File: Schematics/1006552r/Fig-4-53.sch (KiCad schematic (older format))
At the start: 46 parts, among them J1 ConnectorGeneric, U601 D3NOR-+3VDC-0VDC-nd1021041-_B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, U602 D3NOR-+3VDC-0VDC-nd1021041-_B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, U603 D3NOR-+3VDC-0VDC-nd1021041-_B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, U604 D3NOR-+3VDC-0VDC-nd1021041-AB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, U605 D3NOR-+3VDC-0VDC-nd1021041-AB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, U606 D3NOR-+3VDC-0VDC-nd1021041-AB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, U607 D3NOR-+3VDC-0VDC-nd1021041-CB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, U608 D3NOR-+3VDC-0VDC-nd1021041-_B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, U609 D3NOR-+3VDC-0VDC-nd1021041-AB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, U610 D3NOR-+3VDC-0VDC-nd1021041-AB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, U611 D3NOR-+3VDC-0VDC-nd1021041-_B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, U612 D3NOR-+3VDC-0VDC-nd1021041-_B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, U613 D3NOR-+3VDC-0VDC-nd1021041-CB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, U614 D3NOR-+3VDC-0VDC-nd1021041-_B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, U615 D3NOR-+3VDC-0VDC-nd1021041-AB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, U616 D3NOR-+3VDC-0VDC-nd1021041-_B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, U617 D3NOR-+3VDC-0VDC-nd1021041-_B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, U618 D3NOR-+3VDC-0VDC-nd1021041-_B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, U619 D3NOR-NC-0VDC-expander-nd1021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, U620 D3NOR-+3VDC-0VDC-nd1021041-_B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, U621 D3NOR-+3VDC-0VDC-nd1021041-AB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, U622 D3NOR-+3VDC-0VDC-nd1021041-_B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, U623 D3NOR-+3VDC-0VDC-nd1021041-_B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, U624 D3NOR-+3VDC-0VDC-nd1021041-_B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, U625 D3NOR-+3VDC-0VDC-nd1021041-_B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, U626 D3NOR-+3VDC-0VDC-nd1021041-_B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, U627 D3NOR-+3VDC-0VDC-nd1021041-_B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, U628 D3NOR-NC-0VDC-expander-nd1021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, U629 D3NOR-+3VDC-0VDC-nd1021041-_B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, U630 D3NOR-+3VDC-0VDC-nd1021041-A_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, U631 D3NOR-+3VDC-0VDC-nd1021041-A_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, U632 D3NOR-+3VDC-0VDC-nd1021041-CB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, U633 D3NOR-+3VDC-0VDC-nd1021041-AB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, U634 D3NOR-+3VDC-0VDC-nd1021041-_B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, U635 D3NOR-+3VDC-0VDC-nd1021041-CB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, U636 D3NOR-+3VDC-0VDC-nd1021041-_B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, U637 D3NOR-+3VDC-0VDC-nd1021041-AB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, U638 D3NOR-+3VDC-0VDC-nd1021041-_B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, U639 D3NOR-NC-0VDC-expander-nd1021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, U640 D3NOR-+3VDC-0VDC-nd1021041-_B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, U641 D3NOR-+3VDC-0VDC-nd1021041-CB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, U642 D3NOR-+3VDC-0VDC-nd1021041-AB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, U643 D3NOR-+3VDC-0VDC-nd1021041-_B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, U644 D3NOR-+3VDC-0VDC-nd1021041-_B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, U645 D3NOR-NC-0VDC-expander-nd1021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

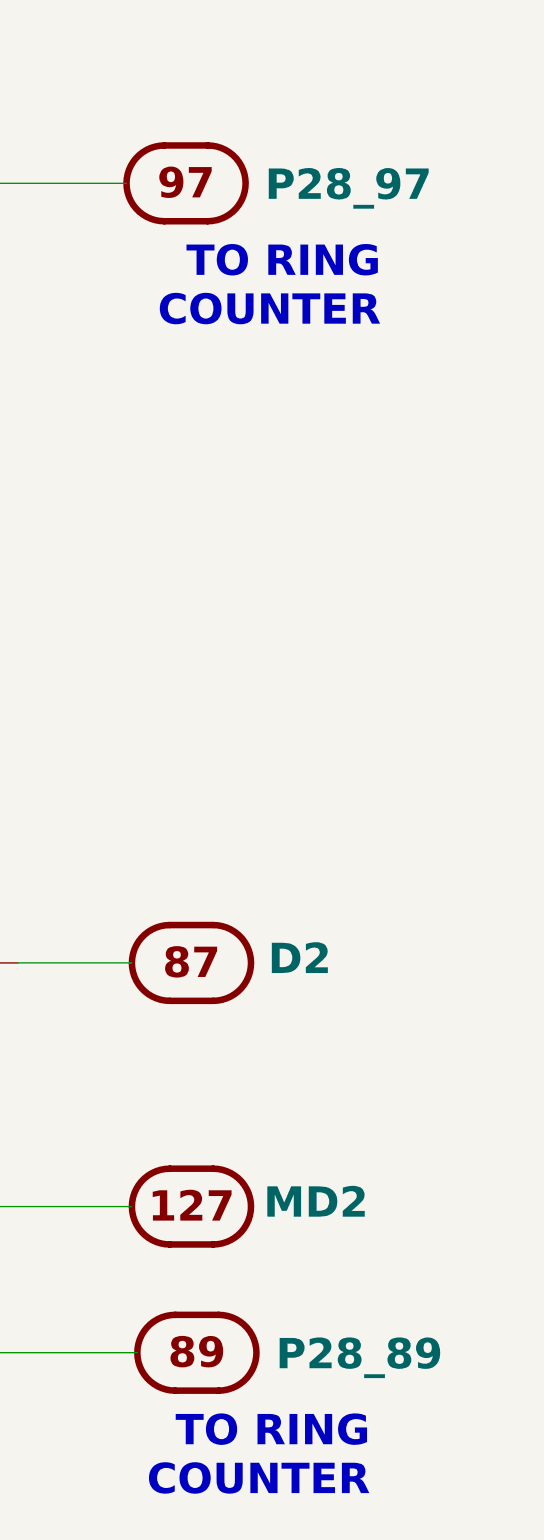
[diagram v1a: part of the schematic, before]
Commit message: In the Block I schematics, for connector pads whose nets weren't named by ND-1021041, I had been provisionally assigning unique names constructed from the module number and pad number, and then maintaining a separate list (connectionsBlockI.txt) to associated these into nets. That didn't work as well as I anticipated.  I've replaced those unique names that varied by pin with unique names that vary instead by net, and have eliminated the now-obsolete connectionsBlockI.txt. Serendipitously, in this process, I also found a couple of nets that I had goofed up, as well as a couple of likely errors in ND-1021041.
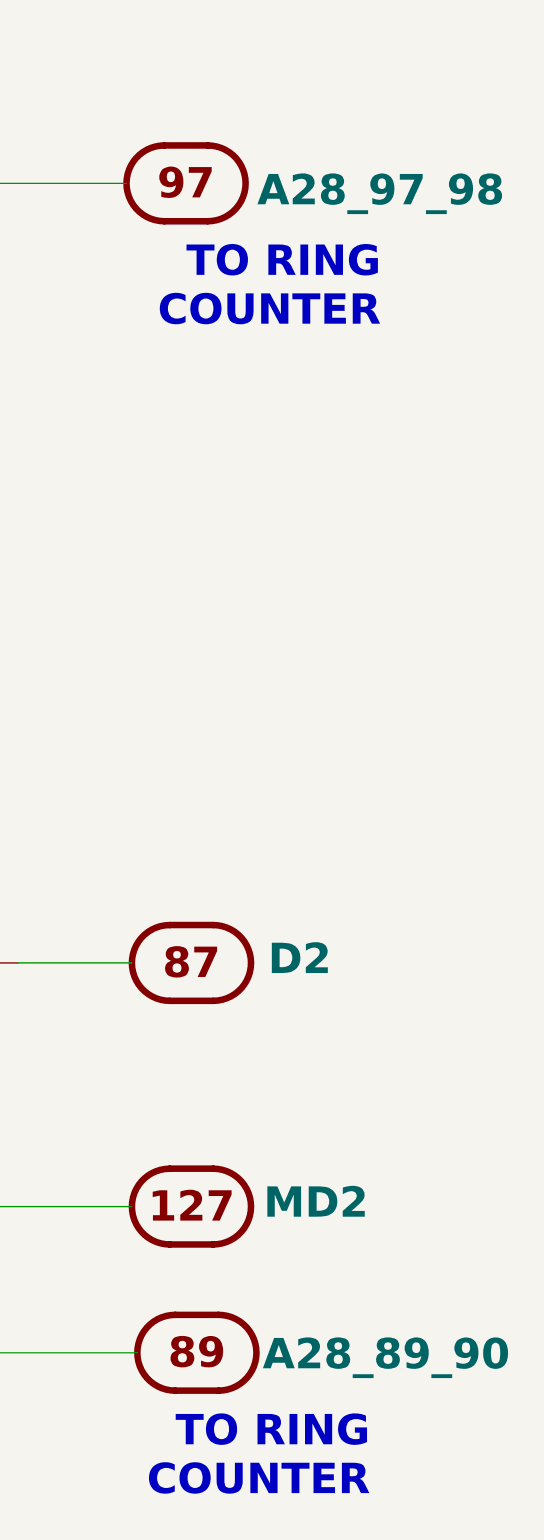
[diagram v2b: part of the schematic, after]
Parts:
- J1: Caption P28_89 -> A28_89_90
- J1: Caption P28_97 -> A28_97_98
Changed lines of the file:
@@
 Sheet 6 7
 Title "BLOCK I LOGIC FLOW N, MODULE A28, DRAWING 1006552"
-Date "2018-11-18"
+Date "2018-11-23"
 Rev "Draft"
 Comp ""
@@
 F 2 "" H 42050 20375 140 0001 C CNN
 F 3 "" H 42050 20375 140 0001 C CNN
-F 4 "P28_89" H 41300 19825 140 0000 C BNB "Caption"
+F 4 "A28_89_90" H 41175 19825 140 0000 C BNB "Caption"
 	89   42050 19900
 	-1   0    0    1
@@
 F 2 "" H 42000 14975 140 0001 C CNN
 F 3 "" H 42000 14975 140 0001 C CNN
-F 4 "P28_97" H 41250 14425 140 0000 C BNB "Caption"
+F 4 "A28_97_98" H 41100 14450 140 0000 C BNB "Caption"
 	97   42000 14500
 	-1   0    0    1

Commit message: When I started recovering transcribed Block I schematics from document ND-1021041, there was no info available to me on the pinout of the NOR-gates they used, and it didn't occur to me that any might be forthcoming, so I chose a pinout arbitrarily.  It turns out that we now have the required info (SCD 1006771), and my arbitrary choices were wrong. I've therefore updated the NOR-library generator script, the relevant NOR libraries themselves, and all of the so-far-recovered Block I schematics using those gates.  It doesn't really matter in the cosmic sense, since the real Block I schematics have become available in the meantime, so that these recovered schematics are of less interest, but it will come in handy when I eventually want to do cross-checking.  I haven't checked these updated schematics in full detail, but I've spot-checked them, and run some ERCs and netlists, and it looks good to me.
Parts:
- U601, U602, U603, U608, U611, U612, U614, U616, U617, U618, U620, U622, U623, U624, U625, U626, U627, U629, U634, U636, U638, U640, U643, U644: value D3NOR-+3VDC-0VDC-nd1021041-_B_-___ -> D3NOR-+3VDC-0VDC-nd1021041-_3_-___; symbol D3NOR-+3VDC-0VDC-nd1021041:D3NOR-+3VDC-0VDC-nd1021041-_B_-___ -> D3NOR-+3VDC-0VDC-nd1021041:D3NOR-+3VDC-0VDC-nd1021041-_3_-___
- U604, U605, U609, U610, U621: value D3NOR-+3VDC-0VDC-nd1021041-ABC-___ -> D3NOR-+3VDC-0VDC-nd1021041-135-___; symbol D3NOR-+3VDC-0VDC-nd1021041:D3NOR-+3VDC-0VDC-nd1021041-ABC-___ -> D3NOR-+3VDC-0VDC-nd1021041:D3NOR-+3VDC-0VDC-nd1021041-135-___
- U606, U615, U633, U637, U642: value D3NOR-+3VDC-0VDC-nd1021041-AB_-___ -> D3NOR-+3VDC-0VDC-nd1021041-13_-___; symbol D3NOR-+3VDC-0VDC-nd1021041:D3NOR-+3VDC-0VDC-nd1021041-AB_-___ -> D3NOR-+3VDC-0VDC-nd1021041:D3NOR-+3VDC-0VDC-nd1021041-13_-___
- U607, U613, U632, U635, U641: value D3NOR-+3VDC-0VDC-nd1021041-CB_-___ -> D3NOR-+3VDC-0VDC-nd1021041-53_-___; symbol D3NOR-+3VDC-0VDC-nd1021041:D3NOR-+3VDC-0VDC-nd1021041-CB_-___ -> D3NOR-+3VDC-0VDC-nd1021041:D3NOR-+3VDC-0VDC-nd1021041-53_-___
- U619, U628, U639, U645: value D3NOR-NC-0VDC-expander-nd1021041-_B_-___ -> D3NOR-NC-0VDC-expander-nd1021041-_3_-___; symbol D3NOR-NC-0VDC-expander-nd1021041:D3NOR-NC-0VDC-expander-nd1021041-_B_-___ -> D3NOR-NC-0VDC-expander-nd1021041:D3NOR-NC-0VDC-expander-nd1021041-_3_-___
- U630, U631: value D3NOR-+3VDC-0VDC-nd1021041-A_C-___ -> D3NOR-+3VDC-0VDC-nd1021041-1_5-___; symbol D3NOR-+3VDC-0VDC-nd1021041:D3NOR-+3VDC-0VDC-nd1021041-A_C-___ -> D3NOR-+3VDC-0VDC-nd1021041:D3NOR-+3VDC-0VDC-nd1021041-1_5-___
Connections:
- net +3VDC: now also U601.8 (+3VDC), U602.8 (+3VDC), U603.8 (+3VDC), U604.8 (+3VDC), U605.8 (+3VDC), U606.8 (+3VDC), U607.8 (+3VDC), U608.8 (+3VDC), U609.8 (+3VDC), U610.8 (+3VDC), U611.8 (+3VDC), U612.8 (+3VDC), U613.8 (+3VDC), U614.8 (+3VDC), U615.8 (+3VDC), U616.8 (+3VDC), U617.8 (+3VDC), U618.8 (+3VDC), U620.8 (+3VDC), U621.8 (+3VDC), U622.8 (+3VDC), U623.8 (+3VDC), U624.8 (+3VDC), U625.8 (+3VDC), U626.8 (+3VDC), U627.8 (+3VDC), U629.8 (+3VDC), U630.8 (+3VDC), U631.8 (+3VDC), U632.8 (+3VDC), U633.8 (+3VDC), U634.8 (+3VDC), U635.8 (+3VDC), U636.8 (+3VDC), U637.8 (+3VDC), U638.8 (+3VDC), U640.8 (+3VDC), U641.8 (+3VDC), U642.8 (+3VDC), U643.8 (+3VDC), U644.8 (+3VDC); no longer U601.6 (+3VDC), U602.6 (+3VDC), U603.6 (+3VDC), U604.6 (+3VDC), U605.6 (+3VDC), U606.6 (+3VDC), U607.6 (+3VDC), U608.6 (+3VDC), U609.6 (+3VDC), U610.6 (+3VDC), U611.6 (+3VDC), U612.6 (+3VDC), U613.6 (+3VDC), U614.6 (+3VDC), U615.6 (+3VDC), U616.6 (+3VDC), U617.6 (+3VDC), U618.6 (+3VDC), U620.6 (+3VDC), U621.6 (+3VDC), U622.6 (+3VDC), U623.6 (+3VDC), U624.6 (+3VDC), U625.6 (+3VDC), U626.6 (+3VDC), U627.6 (+3VDC), U629.6 (+3VDC), U630.6 (+3VDC), U631.6 (+3VDC), U632.6 (+3VDC), U633.6 (+3VDC), U634.6 (+3VDC), U635.6 (+3VDC), U636.6 (+3VDC), U637.6 (+3VDC), U638.6 (+3VDC), U640.6 (+3VDC), U641.6 (+3VDC), U642.6 (+3VDC), U643.6 (+3VDC), U644.6 (+3VDC)
- net 0VDC: now also U601.1 (0VDC), U602.1 (0VDC), U603.1 (0VDC), U604.4 (0VDC), U605.4 (0VDC), U606.4 (0VDC), U607.1 (0VDC), U608.1 (0VDC), U609.4 (0VDC), U610.4 (0VDC), U611.1 (0VDC), U612.1 (0VDC), U613.1 (0VDC), U614.1 (0VDC), U615.4 (0VDC), U616.1 (0VDC), U617.1 (0VDC), U618.1 (0VDC), U619.1 (0VDC), U620.1 (0VDC), U621.4 (0VDC), U622.1 (0VDC), U623.1 (0VDC), U624.1 (0VDC), U625.1 (0VDC), U626.1 (0VDC), U627.1 (0VDC), U628.1 (0VDC), U629.1 (0VDC), U630.4 (0VDC), U631.4 (0VDC), U632.1 (0VDC), U633.4 (0VDC), U634.1 (0VDC), U635.1 (0VDC), U636.1 (0VDC), U637.4 (0VDC), U638.1 (0VDC), U639.1 (0VDC), U640.1 (0VDC), U641.1 (0VDC), U642.4 (0VDC), U643.1 (0VDC), U644.1 (0VDC), U645.1 (0VDC); no longer U601.2 (0VDC), U602.2 (0VDC), U603.2 (0VDC), U604.5 (0VDC), U605.5 (0VDC), U606.2 (0VDC), U607.5 (0VDC), U608.2 (0VDC), U609.5 (0VDC), U610.5 (0VDC), U611.2 (0VDC), U612.2 (0VDC), U613.5 (0VDC), U614.2 (0VDC), U615.2 (0VDC), U616.2 (0VDC), U617.2 (0VDC), U618.2 (0VDC), U619.2 (0VDC), U620.2 (0VDC), U621.5 (0VDC), U622.2 (0VDC), U623.2 (0VDC), U624.2 (0VDC), U625.2 (0VDC), U626.2 (0VDC), U627.2 (0VDC), U628.2 (0VDC), U629.2 (0VDC), U630.5 (0VDC), U631.5 (0VDC), U632.5 (0VDC), U633.2 (0VDC), U634.2 (0VDC), U635.5 (0VDC), U636.2 (0VDC), U637.2 (0VDC), U638.2 (0VDC), U639.2 (0VDC), U640.2 (0VDC), U641.5 (0VDC), U642.2 (0VDC), U643.2 (0VDC), U644.2 (0VDC), U645.2 (0VDC)
- net at U610.3, U611.3: now also U606.7, U607.5; no longer U606.1 (J), U607.2 (C)
- net at U606.3, U608.3: now also U605.7, U610.5; no longer U605.1 (J), U610.2 (C)
- net at U604.3, U614.3, U615.3: now also U610.7; no longer U610.1 (J)
- net at J1.103, J1.21, U620.3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: now also U605.5, U613.7, U615.1; no longer U605.2 (C), U613.1 (J), U615.4 (A)
- net at U605.3, U612.3, U613.3: now also U609.7; no longer U609.1 (J)
- net at U602.3: now also U601.7; no longer U601.1 (J)
- net at J1.43: now also U608.7; no longer U608.1 (J)
- net at J1.27: now also U628.7; no longer U628.1 (J)
- net at J1.19, U628.3: now also U620.7; no longer U620.1 (J)
- net at J1.61, U622.3, U623.3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: now also U618.7; no longer U618.1 (J)
- net at J1.81: now also U638.7; no longer U638.1 (J)
- net at U637.3, U638.3: now also U632.5, U633.7; no longer U632.2 (C), U633.1 (J)
- net at J1.41: now also U619.7; no longer U619.1 (J)
- net at U626.3, U627.3: now also U621.7; no longer U621.1 (J)
- net at U621.2 (NC): no longer J1.51
- net at U642.3, U643.3: now also U637.7; no longer U637.1 (J)
- net at U631.1: now also J1.63, U622.7, U623.7, U630.5; no longer U633.3 (B)
- net at U634.3, U635.3, U636.3: now also U632.7, U633.1; no longer U632.1 (J), U633.4 (A)
- net at J1.37, U616.3, U617.3: now also U611.7; no longer U611.1 (J)
- net at J1.89: now also U643.7; no longer U643.1 (J)
- net at J1.127: now also U645.7; no longer U645.1 (J)
- net at J1.77, U639.3: now also U634.7, U636.7; no longer U634.1 (J), U636.1 (J)
- net at J1.67: now also U639.7; no longer U639.1 (J)
- net at J1.97: now also U640.7; no longer U640.1 (J)
- net at U640.3, U641.3: now also U635.7; no longer U635.1 (J)
- net at J1.101: now also U629.7; no longer U629.1 (J)
- net at J1.33: now also U616.7; no longer U616.1 (J)
- net at U630.1: now also U641.5, U642.7, U644.3, U645.3; no longer U632.3 (B)
- net at J1.59, U618.3: now also U612.7; no longer U612.1 (J)
- net at J1.29, U619.3: now also U617.7; no longer U617.1 (J)
- net at J1.87: now also U644.7; no longer U644.1 (J)
- new net: U604.7, U607.3, U609.1
- new net: U606.1, U607.7, U609.3
- new net: U604.1, U613.5, U615.7
- new net: U602.7, U603.3, U604.5, U605.1
- new net: U603.7, U609.5, U610.1
- new net: J1.93, U614.7, U621.1, U635.5, U637.1
- new net: J1.51, U621.5
- new net: U631.7, U633.3
- new net: U631.5, U641.7, U642.1
- new net: J1.53, U624.7, U625.7
- new net: U630.7, U632.3
- new net: J1.55, U626.7, U627.7
- now unconnected: U604.2 (C), U609.2 (C), U613.2 (C), U630.2 (C), U631.2 (C), U635.2 (C), U641.2 (C)

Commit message: Transcription of 1006552A (Block I AGC module A28) to CAD has been completed, the semi-automated comparison to 1006552r has been made, errors detected in those two implementations have been corrected where it makes sense to do so, and the residual unresolvable discrepancies have been documented in README.md.
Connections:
- net at J1.21, U605.5, U613.7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: no longer J1.103, U629.3
- new net: J1.103, U629.3
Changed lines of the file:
@@
 Wire Wire Line
 	20950 15750 20275 15750
-Wire Wire Line
-	17725 15750 17725 16575
 Connection ~ 17725 16575
 Wire Wire Line
@@
 Wire Wire Line
 	20275 15500 20275 15750
-Connection ~ 20275 15750
-Wire Wire Line
-	20275 15750 17725 15750
 Wire Wire Line
 	20225 17350 20225 18250
@@
 Text Notes 42850 20575 2    140  ~ 28
 TO RING\nCOUNTER
+Wire Notes Line
+	19950 15300 19700 15300
+Wire Notes Line
+	19700 15300 19700 16250
+Wire Notes Line
+	19700 16250 23650 16250
+Wire Notes Line
+	23650 16250 23650 16400
 $EndSCHEMATC

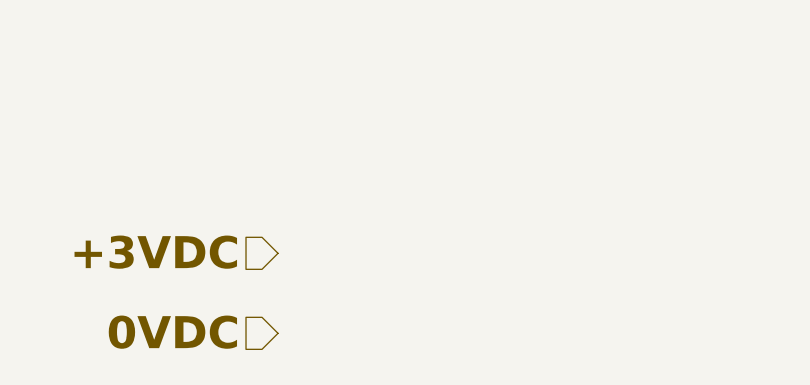
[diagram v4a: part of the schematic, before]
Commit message: Made visual fixes using eelint, and some electrical changes that shouldn't affect the netlist in order to accommodate new KiCad ERC features.  The ERC passes.  The netlist was not previously in the repository, but has now been added.
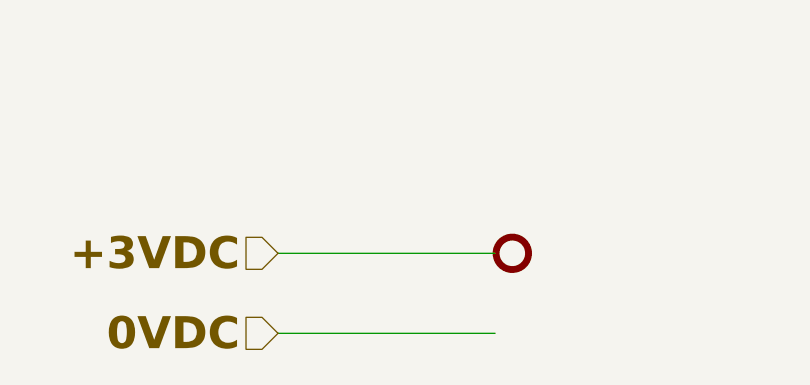
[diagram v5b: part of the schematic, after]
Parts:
- added N601, N602: Node2, symbol AGC_DSKY:Node2
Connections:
- net +3VDC: now also N601.1
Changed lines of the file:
@@
-EESchema Schematic File Version 4
+EESchema Schematic File Version 5
 LIBS:module-cache
 EELAYER 29 0
@@
 Wire Notes Line
 	23650 16250 23650 16400
+$Comp
+L AGC_DSKY:Node2 N601
+U 1 1 5CD61FFE
+P 3575 29075
+F 0 "N601" H 3575 29175 50  0001 C CNN
+F 1 "Node2" H 3575 29250 50  0001 C CNN
+F 2 "" H 3575 29075 50  0001 C CNN
+F 3 "" H 3575 29075 50  0001 C CNN
+F 4 "+3VDC" H 3500 29075 140 0001 R CNB "Caption"
+	1    3575 29075
+	-1   0    0    1
+$EndComp
+$Comp
+L AGC_DSKY:Node2 N602
+U 1 0 5CD6276C
+P 3575 29425
+F 0 "N602" H 3575 29525 50  0001 C CNN
+F 1 "Node2" H 3575 29600 50  0001 C CNN
+F 2 "" H 3575 29425 50  0001 C CNN
+F 3 "" H 3575 29425 50  0001 C CNN
+F 4 "0VDC" H 3500 29425 140 0001 R CNB "Caption"
+	1    3575 29425
+	-1   0    0    1
+$EndComp
+Wire Wire Line
+	2550 29075 3500 29075
+Wire Wire Line
+	2550 29425 3500 29425
 $EndSCHEMATC
